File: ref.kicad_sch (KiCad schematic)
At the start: 45 parts, among them Q61 BSS139, U6 REF7050, U61 OPA2189DGK, U62 OPA828DGN

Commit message: Adjust placements
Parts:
- added C73: 10n, Capacitor_SMD:C_0603_1608Metric, symbol Device:C
- added R72: 330, Resistor_SMD:R_0402_1005Metric, symbol Device:R
- C71: value 10n -> 330p; LCSC C307500 -> C1664
- R70: value 100 -> 10; LCSC (none) -> C25077
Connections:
- net 10V: now also U61.5 (+); no longer R70.2
- net GND: now also C73.2; no longer C71.2
- net Ref10V: now also R70.2, C73.1, R72.2; no longer U61.6 (-), U61.7
- net at C71.1, R70.1: now also U61.7; no longer U61.5 (+)
- new net: C71.2, R72.1, U61.6 (-)
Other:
- moved on the sheet: C6, C67, C68, C69, C70, Q61, R601, R602, R603, R604, R605, R606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

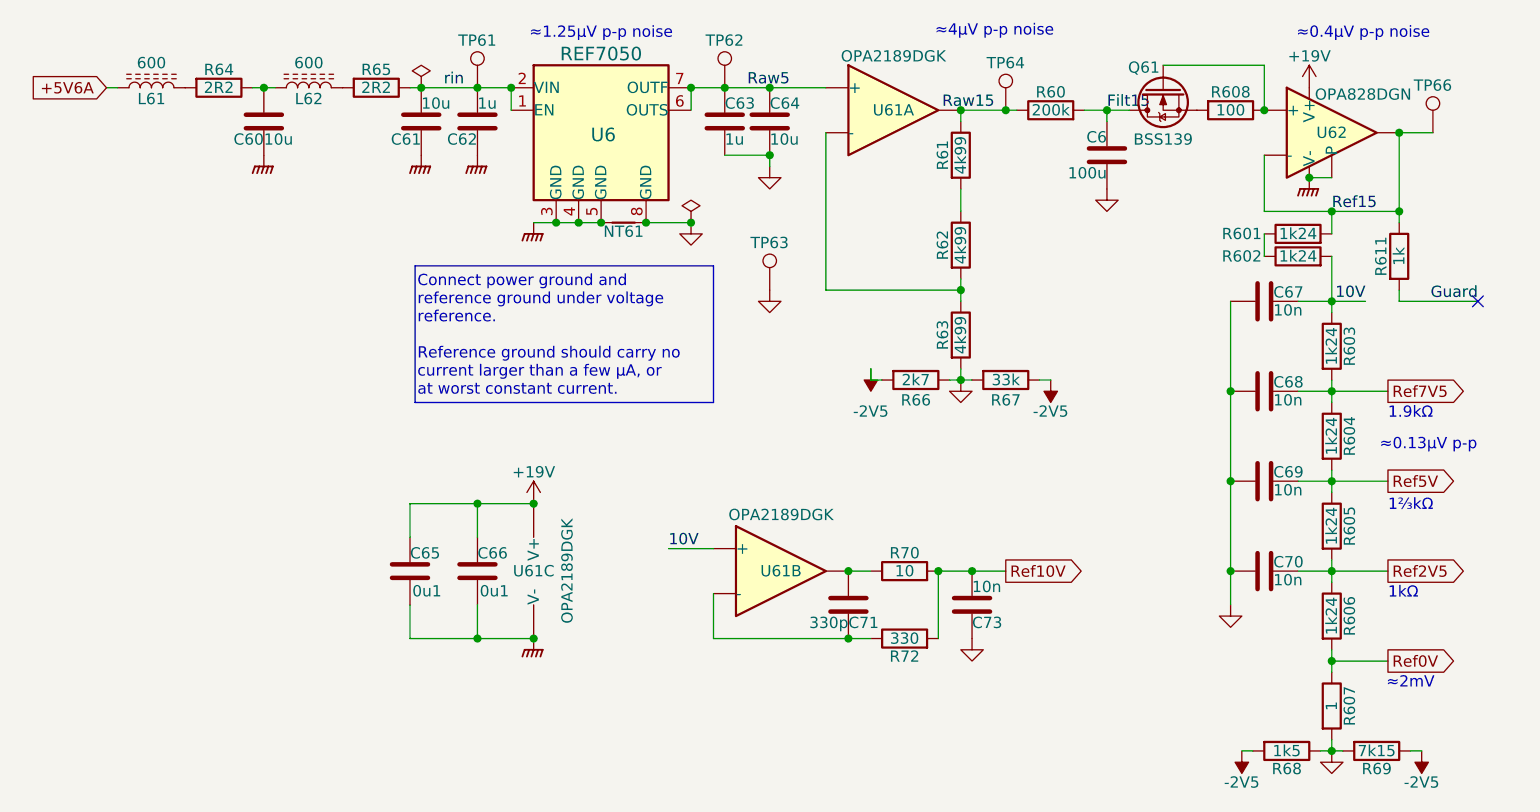
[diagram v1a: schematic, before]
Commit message: Power mostly routed
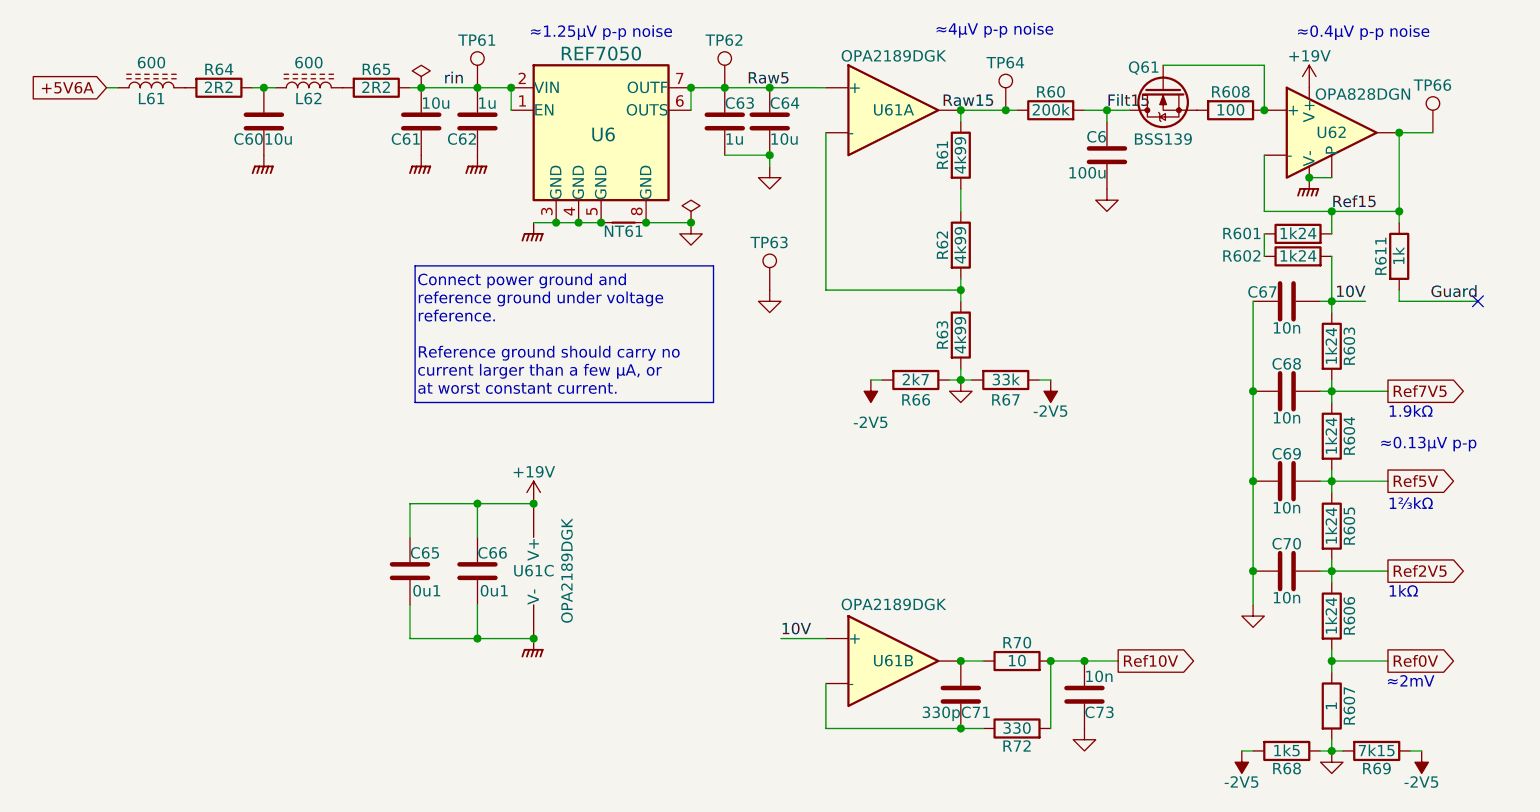
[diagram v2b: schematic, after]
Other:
- moved on the sheet: C67, C68, C69, C70, C71, C73, R70, R72, U61B

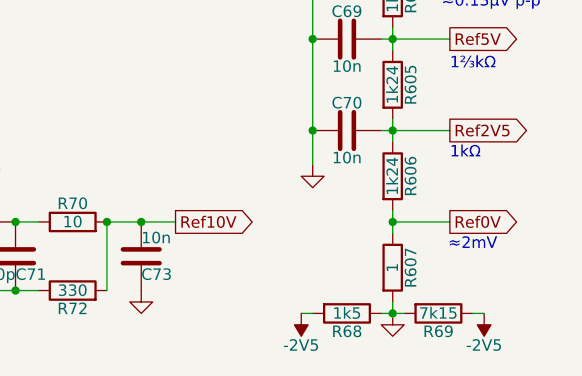
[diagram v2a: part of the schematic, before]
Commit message: Nearly all routed.  Repinning FDA resistors.
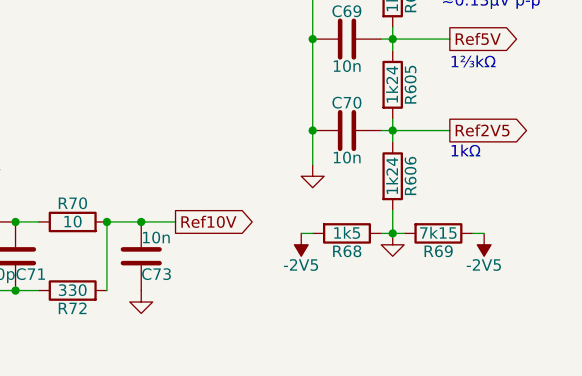
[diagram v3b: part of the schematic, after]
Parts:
- removed R607: 1, Resistor_SMD:R_0603_1608Metric, symbol Device:R
- R608: LCSC (none) -> C25076
- R611: LCSC (none) -> C11702
- R68: footprint Resistor_SMD:R_0402_1005Metric -> Resistor_SMD:R_0603_1608Metric; LCSC C25867 -> (none)
- U62: LCSC (none) -> C20345611
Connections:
- net Ref0V is gone; now on net GND: R606.2
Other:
- note removed: "≈2mV"
- moved on the sheet: R68, R69
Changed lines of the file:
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@@
 		)
 	)
-	(text "≈2mV"
-		(exclude_from_sim no)
-		(at 189.23 119.38 0)
-		(effects
-			(font
-				(size 1.27 1.27)
-			)
-		)
-	)
 	(text "≈1.25µV p-p noise"
 		(exclude_from_sim no)
@@
 	)
 	(junction
-		(at 180.34 116.84)
-		(diameter 0)
-		(color 0 0 0 0)
-	)
-	(junction
 		(at 116.84 52.07)
 		(diameter 0)
@@
 	)
 	(junction
-		(at 180.34 127)
+		(at 180.34 118.11)
 		(diameter 0)
 		(color 0 0 0 0)
@@
 	(wire
 		(pts
-			(xy 180.34 116.84) (xy 186.69 116.84)
-		)
-		(stroke
-			(width 0)
-			(type default)
-		)
-	)
-	(wire
-		(pts
-			(xy 189.23 127) (xy 190.5 127)
+			(xy 189.23 118.11) (xy 190.5 118.11)
 		)
 		(stroke
@@
 	(wire
 		(pts
-			(xy 180.34 127) (xy 181.61 127)
+			(xy 180.34 118.11) (xy 181.61 118.11)
 		)
 		(stroke
@@
 	(wire
 		(pts
-			(xy 180.34 116.84) (xy 180.34 118.11)
+			(xy 180.34 115.57) (xy 180.34 118.11)
 		)
 		(stroke
@@
 	(wire
 		(pts
-			(xy 170.18 127) (xy 171.45 127)
+			(xy 170.18 118.11) (xy 171.45 118.11)
 		)
 		(stroke
@@
 	(wire
 		(pts
-			(xy 180.34 127) (xy 180.34 125.73)
-		)
-		(stroke
-			(width 0)
-			(type default)
-		)
-	)
-	(wire
-		(pts
 			(xy 118.11 114.3) (xy 123.19 114.3)
 		)
@@
 	(wire
 		(pts
-			(xy 180.34 115.57) (xy 180.34 116.84)
-		)
-		(stroke
-			(width 0)
-			(type default)
-		)
-	)
-	(wire
-		(pts
-			(xy 179.07 127) (xy 180.34 127)
+			(xy 179.07 118.11) (xy 180.34 118.11)
 		)
 		(stroke
@@
 		)
 	)
-	(global_label "Ref0V"
-		(shape output)
-		(at 186.69 116.84 0)
-		(effects
-			(font
-				(size 1.27 1.27)
-			)
-			(justify left)
-		)
-		(property "Intersheetrefs" "${INTERSHEET_REFS}"
-			(at 186.69 114.554 0)
-			(effects
-				(font
-					(size 1.27 1.27)
-				)
-				(justify left)
-			)
-		)
-	)
 	(global_label "Ref7V5"
 		(shape output)
@@
 			)
 		)
-		(property "LCSC" ""
+		(property "LCSC" "C25076"
 			(at 168.91 54.61 90)
 			(effects
@@
 	(symbol
 		(lib_id "power:-2V5")
-		(at 190.5 127 180)
+		(at 190.5 118.11 180)
 		(unit 1)
 		(exclude_from_sim no)
@@
 		(dnp no)
 		(property "Reference" "#PWR0122"
-			(at 190.5 123.19 0)
+			(at 190.5 114.3 0)
 			(effects
 				(font
@@
 		)
 		(property "Value" "-2V5"
-			(at 190.5 130.556 0)
+			(at 190.5 121.666 0)
 			(effects
 				(font
@@
 		)
 		(property "Footprint" ""
-			(at 190.5 127 0)
+			(at 190.5 118.11 0)
 			(effects
 				(font
@@
 		)
 		(property "Datasheet" ""
-			(at 190.5 127 0)
+			(at 190.5 118.11 0)
 			(effects
 				(font
@@
 		)
 		(property "Description" "Power symbol creates a global label with name \"-2V5\""
-			(at 190.5 127 0)
+			(at 190.5 118.11 0)
 			(effects
 				(font
@@
 	(symbol
 		(lib_id "power:-2V5")
-		(at 170.18 127 180)
+		(at 170.18 118.11 180)
 		(unit 1)
 		(exclude_from_sim no)
@@
 		(dnp no)
 		(property "Reference" "#PWR0728"
-			(at 170.18 123.19 0)
+			(at 170.18 114.3 0)
 			(effects
 				(font
@@
 		)
 		(property "Value" "-2V5"
-			(at 170.18 130.556 0)
+			(at 170.18 121.666 0)
 			(effects
 				(font
@@
 		)
 		(property "Footprint" ""
-			(at 170.18 127 0)
+			(at 170.18 118.11 0)
 			(effects
 				(font
@@
 		)
 		(property "Datasheet" ""
-			(at 170.18 127 0)
+			(at 170.18 118.11 0)
 			(effects
 				(font
@@
 		)
 		(property "Description" "Power symbol creates a global label with name \"-2V5\""
-			(at 170.18 127 0)
+			(at 170.18 118.11 0)
 			(effects
 				(font
@@
 			)
 		)
-		(property "LCSC" ""
+		(property "LCSC" "C11702"
 			(at 187.96 71.12 90)
 			(effects
@@
 	)
 	(symbol
-		(lib_id "Device:R")
-		(at 180.34 121.92 0)
-		(unit 1)
-		(exclude_from_sim no)
-		(in_bom no)
-		(on_board yes)
-		(dnp no)
-		(property "Reference" "R607"
-			(at 182.372 121.92 90)
-			(effects
-				(font
-					(size 1.27 1.27)
-				)
-			)
-		)
-		(property "Value" "1"
-			(at 180.34 121.92 90)
-			(effects
-				(font
-					(size 1.27 1.27)
-				)
-			)
-		)
-		(property "Footprint" "Resistor_SMD:R_0603_1608Metric"
-			(at 178.562 121.92 90)
-			(effects
-				(font
-					(size 1.27 1.27)
-				)
-				(hide yes)
-			)
-		)
-		(property "Datasheet" "0.1%"
-			(at 180.34 121.92 0)
-			(effects
-				(font
-					(size 1.27 1.27)
-				)
-				(hide yes)
-			)
-		)
-		(property "Description" "Resistor"
-			(at 180.34 121.92 0)
-			(effects
-				(font
-					(size 1.27 1.27)
-				)
-				(hide yes)
-			)
-		)
-		(property "Stock" ""
-			(at 180.34 121.92 90)
-			(effects
-				(font
-					(size 1.27 1.27)
-				)
-				(hide yes)
-			)
-		)
-		(pin "2"
-		)
-		(pin "1"
-		)
-		(instances
-			(project "lincal"
-				(path "/b054cef4-39e3-49d8-aff0-7ba5a206c187/525413b8-c4e9-4b1d-b0c6-ca0be2e26a7f"
-					(reference "R607")
-					(unit 1)
-				)
-			)
-		)
-	)
-	(symbol
 		(lib_id "Parts:OPA828DGN")
 		(at 180.34 57.15 0)
@@
 			)
 		)
+		(property "LCSC" "C20345611"
+			(at 180.34 57.15 0)
+			(effects
+				(font
+					(size 1.27 1.27)
+				)
+				(hide yes)
+			)
+		)
 		(pin "3"
 		)
@@
 	(symbol
 		(lib_id "power:GND")
-		(at 180.34 127 0)
+		(at 180.34 118.11 0)
 		(unit 1)
 		(exclude_from_sim no)
@@
 		(dnp no)
 		(property "Reference" "#PWR0729"
-			(at 180.34 133.35 0)
+			(at 180.34 124.46 0)
 			(effects
 				(font
@@
 		)
 		(property "Value" "GND"
-			(at 180.34 130.81 0)
+			(at 180.34 121.92 0)
 			(effects
 				(font
@@
 		)
 		(property "Footprint" ""
-			(at 180.34 127 0)
+			(at 180.34 118.11 0)
 			(effects
 				(font
@@
 		)
 		(property "Datasheet" ""
-			(at 180.34 127 0)
+			(at 180.34 118.11 0)
 			(effects
 				(font
@@
 		)
 		(property "Description" "Power symbol creates a global label with name \"GND\" , ground"
-			(at 180.34 127 0)
+			(at 180.34 118.11 0)
 			(effects
 				(font
@@
 	(symbol
 		(lib_id "Device:R")
-		(at 185.42 127 270)
+		(at 185.42 118.11 270)
 		(unit 1)
 		(exclude_from_sim no)
@@
 		(dnp no)
 		(property "Reference" "R69"
-			(at 185.42 129.032 90)
+			(at 185.42 120.142 90)
 			(effects
 				(font
@@
 		)
 		(property "Value" "7k15"
-			(at 185.42 127 90)
+			(at 185.42 118.11 90)
 			(effects
 				(font
@@
 		)
 		(property "Footprint" "Resistor_SMD:R_0603_1608Metric"
-			(at 185.42 125.222 90)
+			(at 185.42 116.332 90)
 			(effects
 				(font
@@
 		)
 		(property "Datasheet" "~"
-			(at 185.42 127 0)
+			(at 185.42 118.11 0)
 			(effects
 				(font
@@
 		)
 		(property "Description" "Resistor"
-			(at 185.42 127 0)
+			(at 185.42 118.11 0)
 			(effects
 				(font
@@
 		)
 		(property "LCSC" ""
-			(at 185.42 127 90)
+			(at 185.42 118.11 90)
 			(effects
 				(font
@@
 		)
 		(property "Stock" ""
-			(at 185.42 127 90)
+			(at 185.42 118.11 90)
 			(effects
 				(font
@@
 	(symbol
 		(lib_id "Device:R")
-		(at 175.26 127 270)
+		(at 175.26 118.11 270)
 		(unit 1)
 		(exclude_from_sim no)
@@
 		(dnp no)
 		(property "Reference" "R68"
-			(at 175.26 129.032 90)
+			(at 175.26 120.142 90)
 			(effects
 				(font
@@
 		)
 		(property "Value" "1k5"
-			(at 175.26 127 90)
+			(at 175.26 118.11 90)
 			(effects
 				(font
@@
 			)
 		)
-		(property "Footprint" "Resistor_SMD:R_0402_1005Metric"
-			(at 175.26 125.222 90)
+		(property "Footprint" "Resistor_SMD:R_0603_1608Metric"
+			(at 175.26 116.332 90)
 			(effects
 				(font
@@
 		)
 		(property "Datasheet" "~"
-			(at 175.26 127 0)
+			(at 175.26 118.11 0)
 			(effects
 				(font
@@
 		)
 		(property "Description" "Resistor"
-			(at 175.26 127 0)
+			(at 175.26 118.11 0)
 			(effects
 				(font
@@
 			)
 		)
-		(property "LCSC" "C25867"
-			(at 175.26 127 90)
+		(property "LCSC" ""
+			(at 175.26 118.11 90)
 			(effects
 				(font
@@
 		)
 		(property "Stock" ""
-			(at 175.26 127 90)
+			(at 175.26 118.11 90)
 			(effects
 				(font

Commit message: DRC update.  Repin ADC.  De-crack the S/H ground.
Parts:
- TP61: value TestPoint -> RefIn
- TP62: value TestPoint -> Raw5
- TP63: value TestPoint -> GND
- TP64: value TestPoint -> Raw15
- TP66: value TestPoint -> Ref15
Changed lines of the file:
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@@
 			)
 		)
-		(property "Value" "TestPoint"
+		(property "Value" "Ref15"
 			(at 191.77 52.07 0)
 			(effects
@@
 			)
 		)
-		(property "Value" "TestPoint"
+		(property "Value" "RefIn"
 			(at 83.82 46.99 0)
 			(effects
@@
 			)
 		)
-		(property "Value" "TestPoint"
+		(property "Value" "Raw5"
 			(at 111.76 46.99 0)
 			(effects
@@
 			)
 		)
-		(property "Value" "TestPoint"
+		(property "Value" "Raw15"
 			(at 143.51 49.53 0)
 			(effects
@@
 			)
 		)
-		(property "Value" "TestPoint"
+		(property "Value" "GND"
 			(at 116.84 69.85 0)
 			(effects

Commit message: Redo the reference ground star point.
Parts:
- NT61: value NetTie_2 -> NetTie_5; footprint Parts:NetTie-2_SMD_Pad0.5mm -> Parts:NetTie-circ; symbol Parts:NetTie_2 -> Parts:NetTie_5
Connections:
- net GND: now also C60.2, C61.2
- net GNDPWR: now also NT61.5; no longer C60.2, C61.2, C62.2, NT61.1, U6.3 (GND), U6.4 (GND), U6.5 (GND)
- new net: C62.2, NT61.1, U6.3 (GND), U6.4 (GND), U6.5 (GND)
- new net AGNDsh1: NT61.4
- new net AGNDsh2: NT61.3

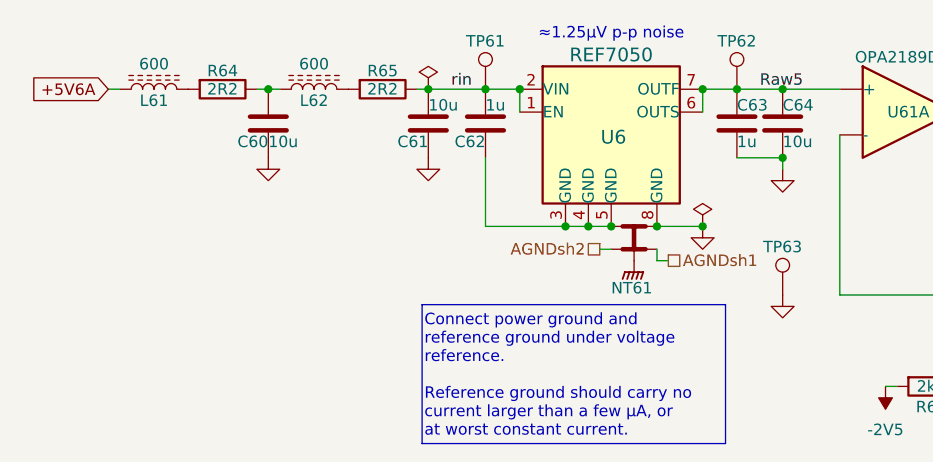
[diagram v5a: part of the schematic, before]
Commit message: Remove placebo planes.  Tidy some analog routing.
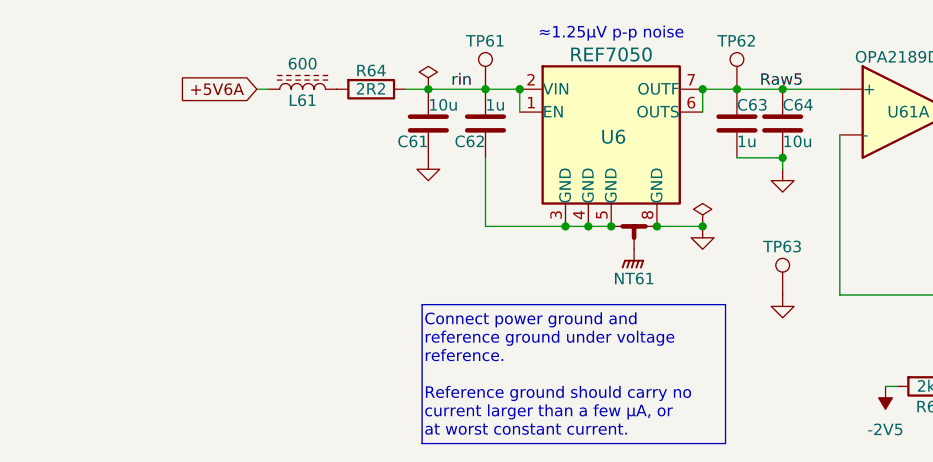
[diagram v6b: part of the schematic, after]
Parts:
- removed C60: 10u, Capacitor_SMD:C_0603_1608Metric, symbol Device:C
- removed L62: 600, Inductor_SMD:L_0603_1608Metric, symbol Device:L_Ferrite
- removed R65: 2R2, Resistor_SMD:R_0603_1608Metric, symbol Device:R
- NT61: value NetTie_5 -> NetTie_3_Tee; symbol Parts:NetTie_5 -> Device:NetTie_3_Tee
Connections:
- net AGNDsh2 is gone; now on net GNDPWR: NT61.3
- net GNDPWR: no longer NT61.5
- net rin: now also R64.1
- removed net AGNDsh1: NT61.4
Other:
- moved on the sheet: L61, R64
